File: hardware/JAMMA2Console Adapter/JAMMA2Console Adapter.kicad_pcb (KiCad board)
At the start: 2 copper layers, 44 x 60 mm, 3 parts, among them J1 KF141R-2.54-7P, J2 KF141R-2.54-7P, J4 DS1037-15MNCKT74-0CC

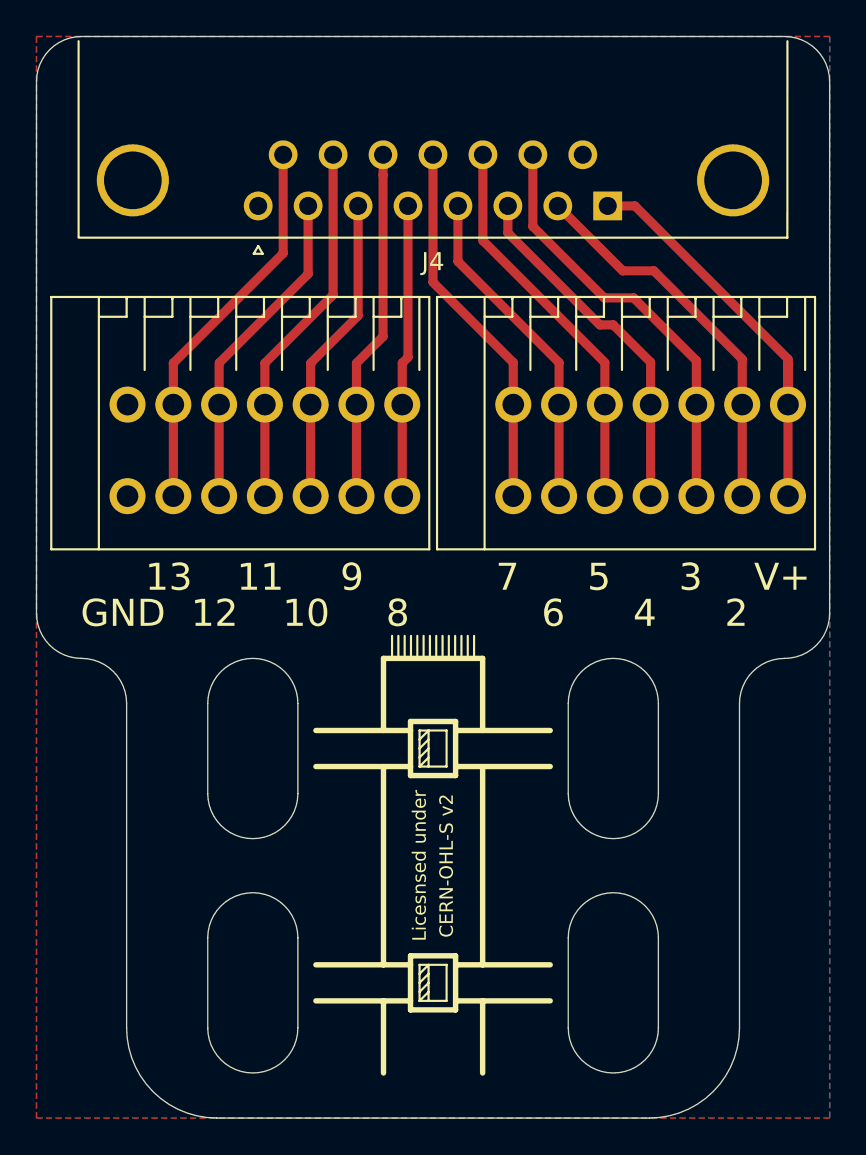
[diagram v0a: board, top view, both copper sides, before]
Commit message: Started major rework on the Audio section (chose the wrong amplifier as it can't drive 4Ohm loads) Moved over to nightly Kicad v 5.9 versions. Was a mistake to do, but will look into reverting another time.
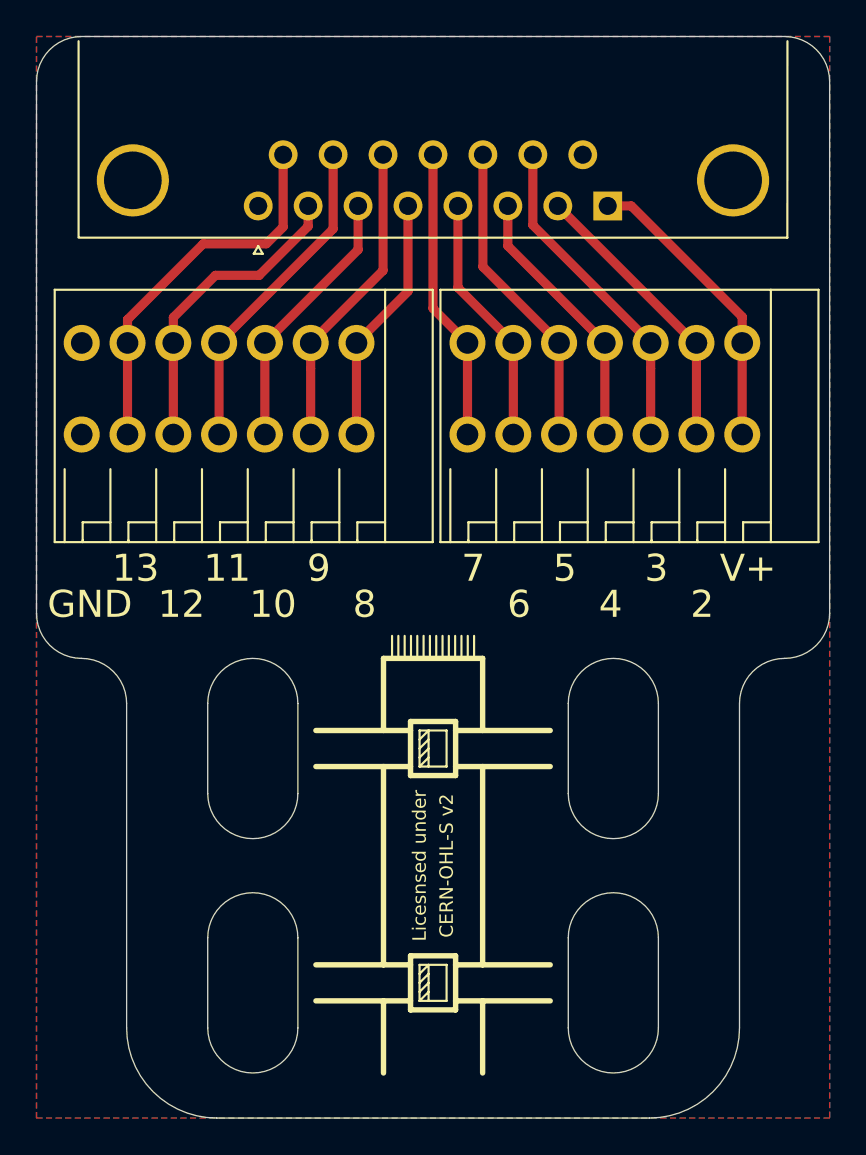
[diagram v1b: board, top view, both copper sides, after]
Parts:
- moved J1 8.50 mm to (165.3, 89.9), turned to 0 degrees
- moved J2 8.50 mm to (143.9, 89.9), turned to 0 degrees
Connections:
- J2 pad 1: Net-(J2-Pad1) -> GND
- J2 pad 7: GND -> Net-(J2-Pad7)
- J4 pad 1: Net-(J1-Pad1) -> Net-(J1-Pad7)
- J4 pad 10: Net-(J1-Pad3) -> Net-(J1-Pad5)
- J4 pad 11: Net-(J1-Pad5) -> Net-(J1-Pad3)
- J4 pad 12: Net-(J1-Pad7) -> Net-(J1-Pad1)
- J4 pad 13: Net-(J2-Pad2) -> Net-(J2-Pad6)
- J4 pad 15: Net-(J2-Pad6) -> Net-(J2-Pad2)
- J4 pad 2: Net-(J1-Pad2) -> Net-(J1-Pad6)
- J4 pad 4: Net-(J1-Pad6) -> Net-(J1-Pad2)
- J4 pad 5: Net-(J2-Pad1) -> Net-(J2-Pad7)
- J4 pad 6: Net-(J2-Pad3) -> Net-(J2-Pad5)
- J4 pad 7: Net-(J2-Pad5) -> Net-(J2-Pad3)
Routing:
- net Net-(J2-Pad1): track 16.2 -> 0.00 mm
- net Net-(J2-Pad7): track 0.00 -> 13.9 mm
- net Net-(J1-Pad2): track 21.4 -> 13.7 mm
- net Net-(J1-Pad1): track 23.2 -> 16.3 mm
- net Net-(J1-Pad3): track 23.4 -> 17.3 mm
- net Net-(J1-Pad4): track 20.5 -> 15.6 mm
- net Net-(J2-Pad6): track 21.5 -> 17.2 mm
- net Net-(J1-Pad7): track 20.6 -> 16.5 mm
- net Net-(J1-Pad5): track 21.5 -> 18.2 mm
- net Net-(J2-Pad5): track 18.1 -> 14.8 mm
- net Net-(J1-Pad6): track 18.2 -> 15.9 mm
- net Net-(J2-Pad4): track 20.5 -> 18.6 mm
- net Net-(J2-Pad2): track 19.6 -> 21.1 mm
